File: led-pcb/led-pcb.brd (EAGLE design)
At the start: 45.7 x 45.7 mm, 9 parts

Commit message: updated pcbs
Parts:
- moved JP2 0.50 mm to (20.3, 30.1)
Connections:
- removed net DOUT: DOUT-12.1, DOUT-16.1, JP2.2
- new net DOUT-12: DOUT-12.1
- new net DOUT-16: DOUT-16.1
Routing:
- net DOUT: track 41.9 -> 0.00 mm
- net GND: track 32.7 -> 62.5 mm, vias 0 -> 2
- net DIN: track 43.2 -> 29.4 mm
- net VCC: track 37.5 -> 40.1 mm
- added copper zone on layer 1, net N$1
- added copper zone on layer 16, net N$2
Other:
- board size 45.7 x 45.7 mm -> 46.7 x 46.7 mm
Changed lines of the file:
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@@
 <setting verticaltext="up"/>
 </settings>
-<grid distance="0.25" unitdist="mm" unit="mm" style="lines" multiple="1" display="no" altdistance="0.025" altunitdist="inch" altunit="mm"/>
+<grid distance="9.84251969" unitdist="mil" unit="mil" style="lines" multiple="1" display="yes" altdistance="0.025" altunitdist="inch" altunit="mm"/>
 <layers>
 <layer number="1" name="Top" color="4" fill="1" visible="yes" active="yes"/>
@@
 <board>
 <plain>
-<circle x="25.4" y="34.29" radius="22.86" width="0.254" layer="20"/>
-<rectangle x1="13.45" y1="33.3" x2="37.45" y2="34.9" layer="20"/>
-<dimension x1="13.45" y1="33.3" x2="13.45" y2="34.9" x3="51.75" y3="34.1" textsize="1.778" layer="1"/>
-<dimension x1="13.45" y1="33.3" x2="37.45" y2="33.3" x3="25.45" y3="60.25" textsize="1.778" layer="1"/>
-<dimension x1="25.428221875" y1="11.43001875" x2="25.371778125" y2="57.14998125" x3="-1.250009375" y3="34.2571" textsize="1.778" layer="1" dtype="diameter"/>
+<circle x="25.4" y="34.29" radius="23.368" width="0.1" layer="20"/>
+<wire x1="17.25" y1="32.75" x2="17.25" y2="35.5" width="0" layer="20"/>
+<wire x1="17.25" y1="35.5" x2="33.5" y2="35.5" width="0" layer="20"/>
+<wire x1="33.5" y1="35.5" x2="33.5" y2="32.75" width="0" layer="20"/>
+<wire x1="33.5" y1="32.75" x2="17.25" y2="32.75" width="0" layer="20"/>
+<dimension x1="25.42976875" y1="10.92201875" x2="25.37023125" y2="57.65798125" x3="-6" y3="34.25" textsize="1.778" layer="25" dtype="diameter"/>
+<dimension x1="17.25" y1="35.5" x2="33.5" y2="35.5" x3="25.375" y3="60" textsize="1.778" layer="25"/>
+<dimension x1="33.5" y1="35.5" x2="33.5" y2="32.75" x3="53.25" y3="34.125" textsize="1.778" layer="25"/>
 </plain>
 <attributes>
@@
 </autorouter>
 <elements>
-<element name="JP2" library="USB3.0" package="1X05" value="" x="20.29" y="30.58"/>
+<element name="JP2" library="USB3.0" package="1X05" value="" x="20.29" y="30.08"/>
 <element name="VCC-16" library="USB3.0" package="1X01" value="M01PTH" x="39.64" y="49.26"/>
 <element name="GND-16" library="USB3.0" package="1X01" value="M01PTH" x="10.16" y="48.76"/>
@@
 <contactref element="VCC-16" pad="1"/>
 <contactref element="VCC-12" pad="1"/>
-<wire x1="30.45" y1="30.58" x2="35.83" y2="30.58" width="0.254" layer="1"/>
-<wire x1="35.83" y1="30.58" x2="40.5" y2="35.25" width="0.254" layer="1"/>
-<wire x1="40.5" y1="35.25" x2="40.5" y2="48.4" width="0.254" layer="1"/>
-<wire x1="40.5" y1="48.4" x2="39.64" y2="49.26" width="0.254" layer="1"/>
-<wire x1="39.64" y1="49.26" x2="37.15" y2="51.75" width="0.254" layer="1"/>
-<wire x1="37.15" y1="51.75" x2="29.48" y2="51.75" width="0.254" layer="1"/>
+<wire x1="30.45" y1="30.08" x2="38.33" y2="30.08" width="0.508" layer="1"/>
+<wire x1="38.33" y1="30.08" x2="41.25" y2="33" width="0.508" layer="1"/>
+<wire x1="41.25" y1="33" x2="41.25" y2="47.65" width="0.508" layer="1"/>
+<wire x1="41.25" y1="47.65" x2="39.64" y2="49.26" width="0.508" layer="1"/>
+<wire x1="39.64" y1="49.26" x2="31.97" y2="49.26" width="0.508" layer="1"/>
+<wire x1="31.97" y1="49.26" x2="29.48" y2="51.75" width="0.508" layer="1"/>
 </signal>
 <signal name="GND">
@@
 <contactref element="GND-16" pad="1"/>
 <contactref element="GND-12" pad="1"/>
-<wire x1="27.91" y1="30.58" x2="26.24" y2="32.25" width="0.254" layer="1"/>
-<wire x1="26.24" y1="32.25" x2="10.5" y2="32.25" width="0.254" layer="1"/>
-<wire x1="10.5" y1="32.25" x2="10.5" y2="42.67" width="0.254" layer="1"/>
-<wire x1="10.5" y1="42.67" x2="13.43" y2="45.6" width="0.254" layer="1"/>
-<wire x1="13.43" y1="45.6" x2="10.16" y2="48.76" width="0" layer="19" extent="1-1"/>
-</signal>
-<signal name="DOUT">
-<contactref element="JP2" pad="2"/>
-<contactref element="DOUT-16" pad="1"/>
+<wire x1="13.43" y1="45.6" x2="13.32" y2="45.6" width="0.254" layer="1"/>
+<wire x1="27.91" y1="30.08" x2="27.83" y2="30.08" width="0.508" layer="1"/>
+<wire x1="27.83" y1="30.08" x2="27.75" y2="30" width="0.508" layer="1"/>
+<wire x1="27.75" y1="30" x2="27.75" y2="29.75" width="0.508" layer="1"/>
+<wire x1="27.75" y1="29.75" x2="29.75" y2="27.75" width="0.508" layer="1"/>
+<wire x1="29.75" y1="27.75" x2="33.75" y2="27.75" width="0.508" layer="1"/>
+<via x="33.75" y="27.75" extent="1-16" drill="0.6" shape="square"/>
+<wire x1="33.75" y1="27.75" x2="33.75" y2="24" width="0.508" layer="16"/>
+<wire x1="33.75" y1="24" x2="33" y2="23.25" width="0.508" layer="16"/>
+<wire x1="33" y1="23.25" x2="12.25" y2="23.25" width="0.508" layer="16"/>
+<wire x1="12.25" y1="23.25" x2="9.5" y2="26" width="0.508" layer="16"/>
+<via x="9.5" y="26" extent="1-16" drill="0.6" shape="square"/>
+<wire x1="9.5" y1="26" x2="9.5" y2="41.67" width="0.508" layer="1"/>
+<wire x1="9.5" y1="41.67" x2="13.43" y2="45.6" width="0.508" layer="1"/>
+<wire x1="13.32" y1="45.6" x2="10.16" y2="48.76" width="0.508" layer="1"/>
+</signal>
+<signal name="DOUT-12">
 <contactref element="DOUT-12" pad="1"/>
-<wire x1="22.83" y1="30.58" x2="20.25" y2="28" width="0.254" layer="1"/>
-<wire x1="20.25" y1="28" x2="20.25" y2="14.75" width="0.254" layer="1"/>
-<wire x1="20.25" y1="14.75" x2="21.72" y2="13.28" width="0.254" layer="1"/>
-<wire x1="21.72" y1="13.28" x2="24.74" y2="13.28" width="0.254" layer="1"/>
-<wire x1="40.16" y1="23.73" x2="40.18" y2="23.75" width="0.254" layer="1"/>
-<wire x1="40.18" y1="23.75" x2="40.25" y2="23.75" width="0.254" layer="1"/>
-<wire x1="40.25" y1="23.75" x2="29.78" y2="13.28" width="0.254" layer="1"/>
-<wire x1="29.78" y1="13.28" x2="24.74" y2="13.28" width="0.254" layer="1"/>
 </signal>
 <signal name="DIN">
@@
 <contactref element="DIN-16" pad="1"/>
 <contactref element="DIN-12" pad="1"/>
-<wire x1="25.37" y1="30.58" x2="27.45" y2="28.5" width="0.254" layer="1"/>
-<wire x1="27.45" y1="28.5" x2="41.75" y2="28.5" width="0.254" layer="1"/>
-<wire x1="41.75" y1="28.5" x2="43.75" y2="26.5" width="0.254" layer="1"/>
-<wire x1="43.75" y1="26.5" x2="43.75" y2="22.75" width="0.254" layer="1"/>
-<wire x1="43.75" y1="22.75" x2="39.78" y2="18.78" width="0.254" layer="1"/>
-<wire x1="39.78" y1="18.78" x2="39.56" y2="18.78" width="0.254" layer="1"/>
-<wire x1="25.37" y1="30.58" x2="23.81" y2="29.02" width="0.254" layer="1"/>
-<wire x1="23.81" y1="29.02" x2="23.81" y2="17.68" width="0.254" layer="1"/>
+<wire x1="25.37" y1="30.08" x2="23.81" y2="28.52" width="0.205" layer="1"/>
+<wire x1="23.81" y1="28.52" x2="23.81" y2="17.68" width="0.205" layer="1"/>
+<wire x1="23.81" y1="17.68" x2="23.81" y2="17.69" width="0.254" layer="1"/>
+<wire x1="23.81" y1="17.69" x2="23.75" y2="17.75" width="0.254" layer="1"/>
+<wire x1="23.75" y1="17.75" x2="38.53" y2="17.75" width="0.254" layer="1"/>
+<wire x1="38.53" y1="17.75" x2="39.56" y2="18.78" width="0.254" layer="1"/>
+</signal>
+<signal name="N$1">
+<polygon width="0.4064" layer="1">
+<vertex x="-13.5" y="64"/>
+<vertex x="63.5" y="64"/>
+<vertex x="63.5" y="7.75"/>
+<vertex x="-11.5" y="7.75"/>
+<vertex x="-11.5" y="8.25"/>
+<vertex x="-13.5" y="8.25"/>
+</polygon>
+</signal>
+<signal name="N$2">
+<polygon width="0.4064" layer="16">
+<vertex x="-13.75" y="64.25"/>
+<vertex x="64" y="64.25"/>
+<vertex x="64" y="6.75"/>
+<vertex x="-13.75" y="6.75"/>
+</polygon>
+</signal>
+<signal name="DOUT-16">
+<contactref element="DOUT-16" pad="1"/>
 </signal>
 </signals>
+<errors>
+</errors>
 </board>
 </drawing>

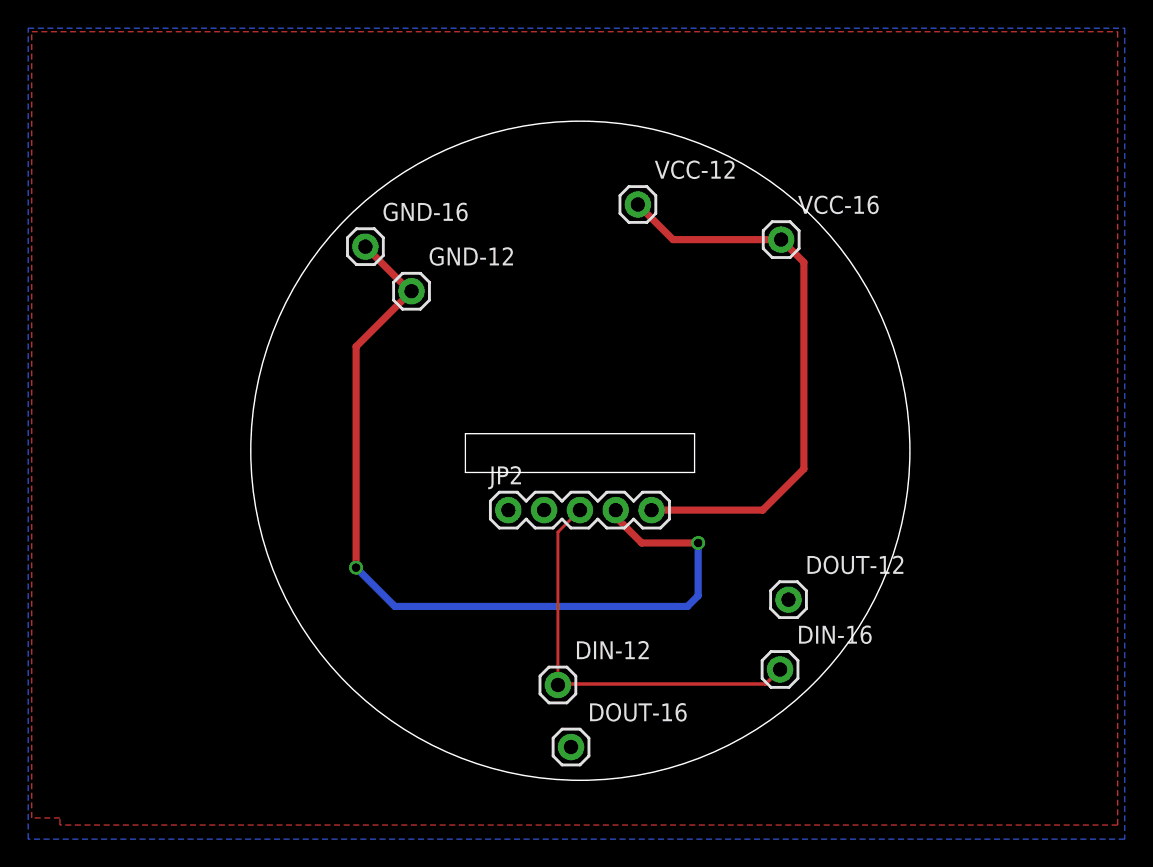
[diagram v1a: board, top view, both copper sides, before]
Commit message: adding bulb-2.brd and bulb-2.sch
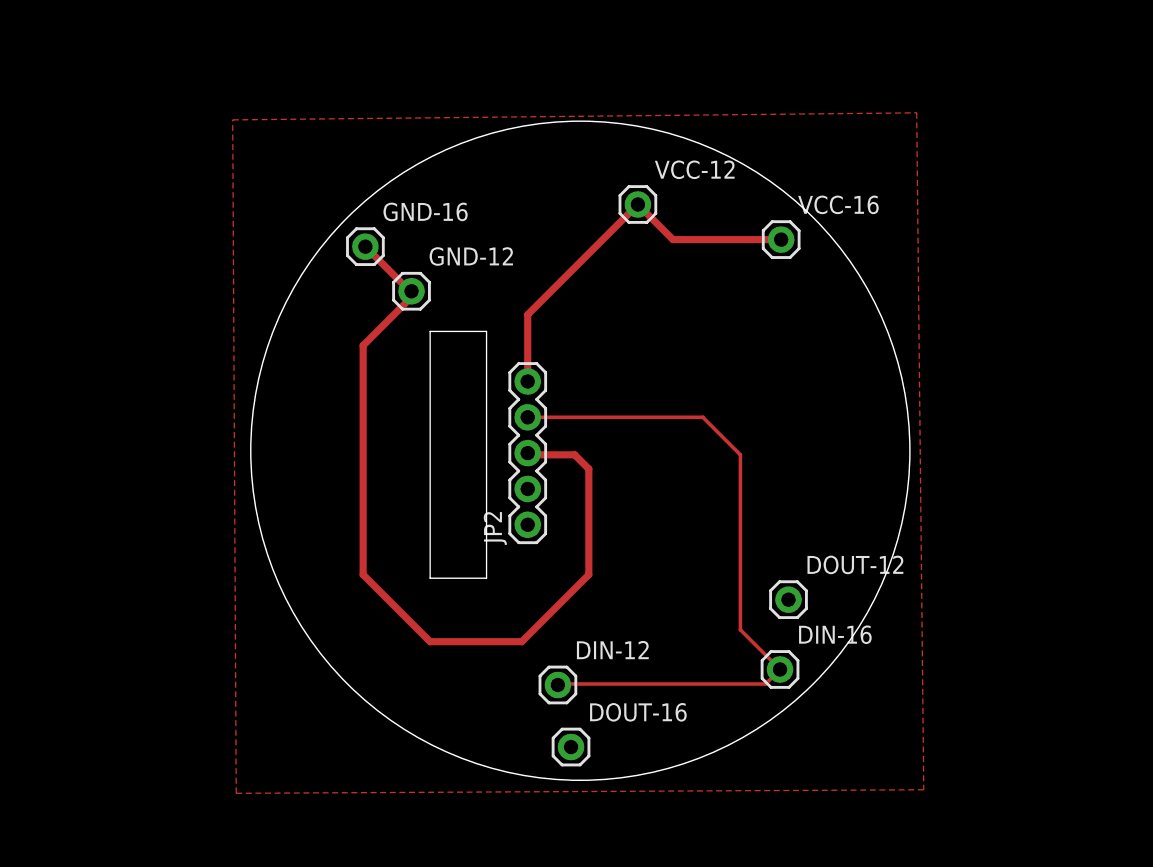
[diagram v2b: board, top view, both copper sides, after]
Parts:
- moved JP2 1.73 mm to (21.7, 29.0), turned to 90 degrees
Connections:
- net DIN: now also JP2.4; no longer JP2.3
- net GND: now also JP2.3; no longer JP2.4
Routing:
- net DIN: track 29.4 -> 49.0 mm
- net VCC: track 40.1 -> 27.4 mm
- net GND: track 62.5 -> 58.4 mm, vias 2 -> 0
- removed copper zone on layer 16, net N$2
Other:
- outline, holes or cut-outs redrawn
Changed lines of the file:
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@@
 <?xml version="1.0" encoding="utf-8"?>
 <!DOCTYPE eagle SYSTEM "eagle.dtd">
-<eagle version="6.5.0">
+<eagle version="7.2.0">
 <drawing>
 <settings>
@@
 <plain>
 <circle x="25.4" y="34.29" radius="23.368" width="0.1" layer="20"/>
-<wire x1="17.25" y1="32.75" x2="17.25" y2="35.5" width="0" layer="20"/>
-<wire x1="17.25" y1="35.5" x2="33.5" y2="35.5" width="0" layer="20"/>
-<wire x1="33.5" y1="35.5" x2="33.5" y2="32.75" width="0" layer="20"/>
-<wire x1="33.5" y1="32.75" x2="17.25" y2="32.75" width="0" layer="20"/>
 <dimension x1="25.42976875" y1="10.92201875" x2="25.37023125" y2="57.65798125" x3="-6" y3="34.25" textsize="1.778" layer="25" dtype="diameter"/>
-<dimension x1="17.25" y1="35.5" x2="33.5" y2="35.5" x3="25.375" y3="60" textsize="1.778" layer="25"/>
-<dimension x1="33.5" y1="35.5" x2="33.5" y2="32.75" x3="53.25" y3="34.125" textsize="1.778" layer="25"/>
+<wire x1="14.75" y1="42.75" x2="18.75" y2="42.75" width="0" layer="20"/>
+<wire x1="18.75" y1="42.75" x2="18.75" y2="25.25" width="0" layer="20"/>
+<wire x1="18.75" y1="25.25" x2="14.75" y2="25.25" width="0" layer="20"/>
+<wire x1="14.75" y1="25.25" x2="14.75" y2="42.75" width="0" layer="20"/>
+<dimension x1="18.75" y1="25.25" x2="14.75" y2="25.25" x3="16.75" y3="6.5" textsize="1.778" layer="25"/>
+<dimension x1="14.75" y1="42.75" x2="14.75" y2="25.25" x3="-0.5" y3="34" textsize="1.778" layer="25"/>
+<dimension x1="18.75" y1="25.25" x2="21.75" y2="25.25" x3="20.25" y3="4" textsize="1.778" layer="25"/>
 </plain>
 <attributes>
@@
 <pass name="Default">
 <param name="RoutingGrid" value="50mil"/>
+<param name="AutoGrid" value="1"/>
+<param name="Efforts" value="0"/>
+<param name="TopRouterVariant" value="1"/>
 <param name="tpViaShape" value="round"/>
 <param name="PrefDir.1" value="|"/>
@@
 </autorouter>
 <elements>
-<element name="JP2" library="USB3.0" package="1X05" value="" x="20.29" y="30.08"/>
+<element name="JP2" library="USB3.0" package="1X05" value="" x="21.67" y="29.04" rot="R90"/>
 <element name="VCC-16" library="USB3.0" package="1X01" value="M01PTH" x="39.64" y="49.26"/>
 <element name="GND-16" library="USB3.0" package="1X01" value="M01PTH" x="10.16" y="48.76"/>
@@
 <signals>
 <signal name="VCC">
-<contactref element="JP2" pad="5"/>
 <contactref element="VCC-16" pad="1"/>
 <contactref element="VCC-12" pad="1"/>
-<wire x1="30.45" y1="30.08" x2="38.33" y2="30.08" width="0.508" layer="1"/>
-<wire x1="38.33" y1="30.08" x2="41.25" y2="33" width="0.508" layer="1"/>
-<wire x1="41.25" y1="33" x2="41.25" y2="47.65" width="0.508" layer="1"/>
-<wire x1="41.25" y1="47.65" x2="39.64" y2="49.26" width="0.508" layer="1"/>
 <wire x1="39.64" y1="49.26" x2="31.97" y2="49.26" width="0.508" layer="1"/>
 <wire x1="31.97" y1="49.26" x2="29.48" y2="51.75" width="0.508" layer="1"/>
+<wire x1="29.75" y1="51.48" x2="29.48" y2="51.75" width="0.508" layer="1"/>
+<contactref element="JP2" pad="5"/>
+<wire x1="21.67" y1="39.2" x2="21.67" y2="43.94" width="0.508" layer="1"/>
+<wire x1="21.67" y1="43.94" x2="29.48" y2="51.75" width="0.508" layer="1"/>
 </signal>
 <signal name="GND">
-<contactref element="JP2" pad="4"/>
 <contactref element="GND-16" pad="1"/>
 <contactref element="GND-12" pad="1"/>
 <wire x1="13.43" y1="45.6" x2="13.32" y2="45.6" width="0.254" layer="1"/>
-<wire x1="27.91" y1="30.08" x2="27.83" y2="30.08" width="0.508" layer="1"/>
-<wire x1="27.83" y1="30.08" x2="27.75" y2="30" width="0.508" layer="1"/>
-<wire x1="27.75" y1="30" x2="27.75" y2="29.75" width="0.508" layer="1"/>
-<wire x1="27.75" y1="29.75" x2="29.75" y2="27.75" width="0.508" layer="1"/>
-<wire x1="29.75" y1="27.75" x2="33.75" y2="27.75" width="0.508" layer="1"/>
-<via x="33.75" y="27.75" extent="1-16" drill="0.6" shape="square"/>
-<wire x1="33.75" y1="27.75" x2="33.75" y2="24" width="0.508" layer="16"/>
-<wire x1="33.75" y1="24" x2="33" y2="23.25" width="0.508" layer="16"/>
-<wire x1="33" y1="23.25" x2="12.25" y2="23.25" width="0.508" layer="16"/>
-<wire x1="12.25" y1="23.25" x2="9.5" y2="26" width="0.508" layer="16"/>
-<via x="9.5" y="26" extent="1-16" drill="0.6" shape="square"/>
-<wire x1="9.5" y1="26" x2="9.5" y2="41.67" width="0.508" layer="1"/>
-<wire x1="9.5" y1="41.67" x2="13.43" y2="45.6" width="0.508" layer="1"/>
 <wire x1="13.32" y1="45.6" x2="10.16" y2="48.76" width="0.508" layer="1"/>
+<contactref element="JP2" pad="3"/>
+<wire x1="13.43" y1="45.07" x2="13.43" y2="45.6" width="0.508" layer="1"/>
+<wire x1="13.43" y1="45.07" x2="13.32" y2="45.07" width="0.508" layer="1"/>
+<wire x1="13.32" y1="45.07" x2="10" y2="41.75" width="0.508" layer="1"/>
+<wire x1="10" y1="41.75" x2="10" y2="25.5" width="0.508" layer="1"/>
+<wire x1="10" y1="25.5" x2="14.75" y2="20.75" width="0.508" layer="1"/>
+<wire x1="14.75" y1="20.75" x2="21.25" y2="20.75" width="0.508" layer="1"/>
+<wire x1="21.25" y1="20.75" x2="26" y2="25.5" width="0.508" layer="1"/>
+<wire x1="26" y1="25.5" x2="26" y2="33" width="0.508" layer="1"/>
+<wire x1="26" y1="33" x2="25" y2="34" width="0.508" layer="1"/>
+<wire x1="25" y1="34" x2="21.79" y2="34" width="0.508" layer="1"/>
+<wire x1="21.79" y1="34" x2="21.67" y2="34.12" width="0.508" layer="1"/>
 </signal>
 <signal name="DOUT-12">
@@
 </signal>
 <signal name="DIN">
-<contactref element="JP2" pad="3"/>
 <contactref element="DIN-16" pad="1"/>
 <contactref element="DIN-12" pad="1"/>
-<wire x1="25.37" y1="30.08" x2="23.81" y2="28.52" width="0.205" layer="1"/>
-<wire x1="23.81" y1="28.52" x2="23.81" y2="17.68" width="0.205" layer="1"/>
 <wire x1="23.81" y1="17.68" x2="23.81" y2="17.69" width="0.254" layer="1"/>
 <wire x1="23.81" y1="17.69" x2="23.75" y2="17.75" width="0.254" layer="1"/>
 <wire x1="23.75" y1="17.75" x2="38.53" y2="17.75" width="0.254" layer="1"/>
 <wire x1="38.53" y1="17.75" x2="39.56" y2="18.78" width="0.254" layer="1"/>
+<wire x1="23.75" y1="17.74" x2="23.81" y2="17.68" width="0.254" layer="1"/>
+<contactref element="JP2" pad="4"/>
+<wire x1="21.67" y1="36.66" x2="34.09" y2="36.66" width="0.254" layer="1"/>
+<wire x1="34.09" y1="36.66" x2="36.75" y2="34" width="0.254" layer="1"/>
+<wire x1="36.75" y1="34" x2="36.75" y2="21.59" width="0.254" layer="1"/>
+<wire x1="36.75" y1="21.59" x2="39.56" y2="18.78" width="0.254" layer="1"/>
 </signal>
 <signal name="N$1">
-<polygon width="0.4064" layer="1">
-<vertex x="-13.5" y="64"/>
-<vertex x="63.5" y="64"/>
-<vertex x="63.5" y="7.75"/>
-<vertex x="-11.5" y="7.75"/>
-<vertex x="-11.5" y="8.25"/>
-<vertex x="-13.5" y="8.25"/>
+<polygon width="0.4064" layer="1" isolate="1.016">
+<vertex x="0.75" y="57.75"/>
+<vertex x="49.25" y="58.25"/>
+<vertex x="49.75" y="10.25"/>
+<vertex x="1" y="10"/>
 </polygon>
 </signal>
-<signal name="N$2">
-<polygon width="0.4064" layer="16">
-<vertex x="-13.75" y="64.25"/>
-<vertex x="64" y="64.25"/>
-<vertex x="64" y="6.75"/>
-<vertex x="-13.75" y="6.75"/>
-</polygon>
-</signal>
